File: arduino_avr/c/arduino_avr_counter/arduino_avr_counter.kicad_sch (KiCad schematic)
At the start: 8 parts, among them SW1 Taster, U1 ICM7555

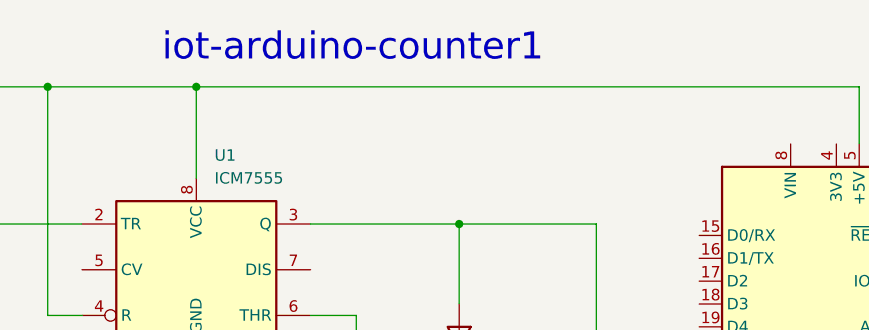
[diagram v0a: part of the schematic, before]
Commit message: Rename project.
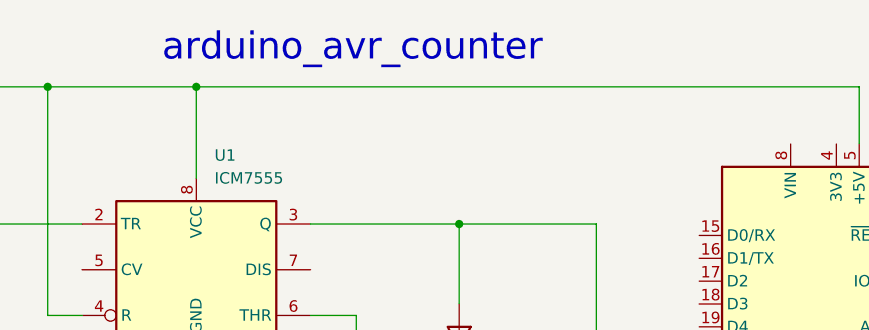
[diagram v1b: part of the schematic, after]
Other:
- note added: "arduino_avr_counter"
- note removed: "iot-arduino-counter1"
- title: iot-arduino-counter1 -> arduino_avr_counter
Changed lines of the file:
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@@
   (paper "A5")
   (title_block
-    (title "iot-arduino-counter1")
+    (title "arduino_avr_counter")
     (date "2022-03-08")
     (rev "1")
@@
     (stroke (width 0) (type default) (color 0 0 0 0))
   )
-  (text "iot-arduino-counter1" (at 77.47 25.4 0)
+  (text "arduino_avr_counter" (at 77.47 25.4 0)
     (effects (font (size 3 3)) (justify left bottom))
   )
